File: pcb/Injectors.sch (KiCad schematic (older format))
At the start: 48 parts, among them Q1 VND14NV04, Q2 VND14NV04, Q3 VND14NV04, Q4 VND14NV04, Q5 VND14NV04, Q6 VND14NV04, Q7 VND14NV04, Q8 VND14NV04

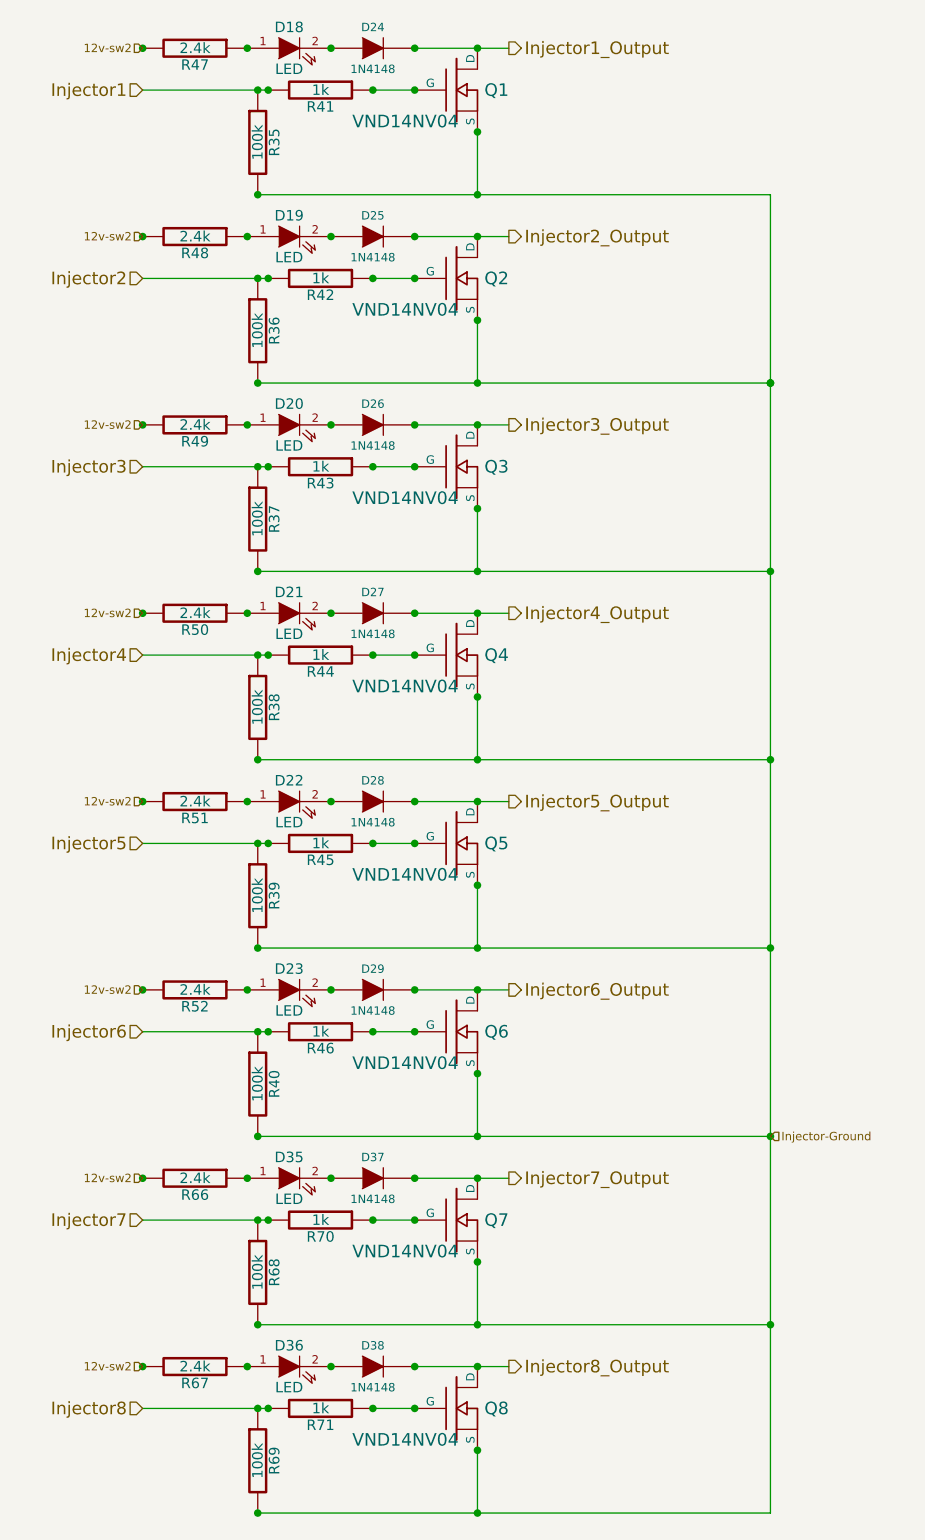
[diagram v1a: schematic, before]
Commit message: Updated schematics, PDFs and PNGs with lumpensack2003 suggestions
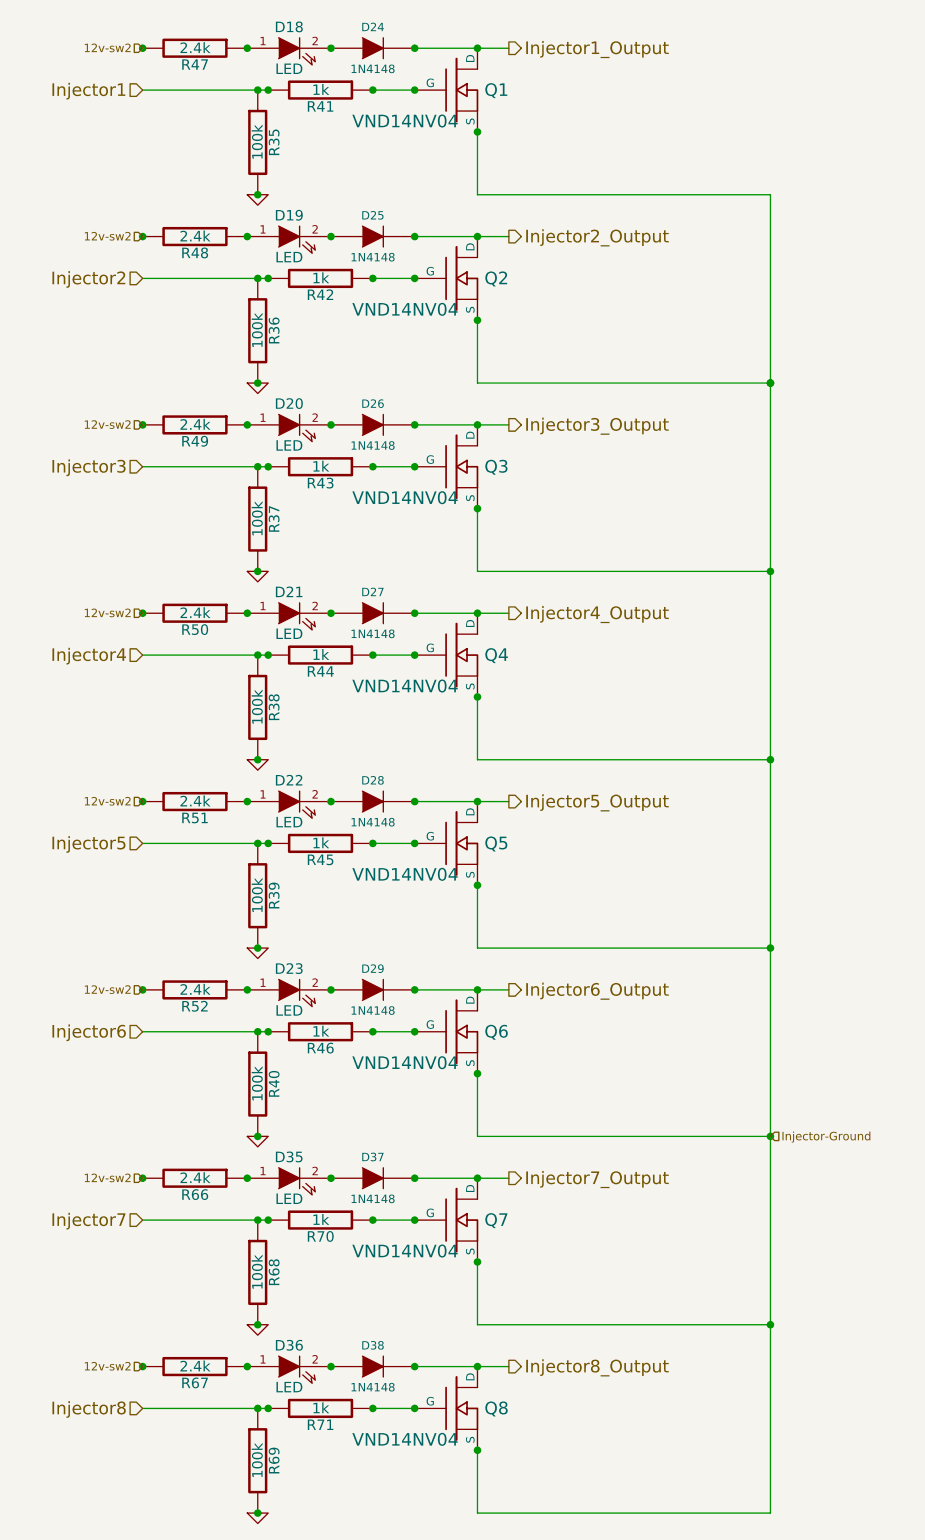
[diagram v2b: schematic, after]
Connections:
- net Injector-Ground: no longer R35.2, R36.2, R37.2, R38.2, R39.2, R40.2, R68.2, R69.2
- new net GND: R35.2, R36.2, R37.2, R38.2, R39.2, R40.2, R68.2, R69.2
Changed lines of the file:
@@
-EESchema Schematic File Version 2  date Sun 05 Feb 2012 11:20:52 AM EST
+EESchema Schematic File Version 2  date Sun 05 Feb 2012 10:59:48 PM EST
+LIBS:opto
+LIBS:Jaguar
 LIBS:power
-LIBS:device
-LIBS:transistors
-LIBS:conn
-LIBS:linear
-LIBS:regul
-LIBS:74xx
-LIBS:analog_switches
-LIBS:interface
-LIBS:opto
-LIBS:contrib
-LIBS:Jaguar
 LIBS:Jaguar-cache
 EELAYER 24  0
@@
 Sheet 6 7
 Title "Jaguar PCB for FreeEMS"
-Date "5 feb 2012"
+Date "6 feb 2012"
 Rev "A.2"
 Comp "diyefi.org"
@@
 Comment4 ""
 $EndDescr
+$Comp
+L GND #PWR063
+U 1 1 4F2F3F04
+P 2950 5000
+F 0 "#PWR063" H 2950 5000 30  0001 C CNN
+F 1 "GND" H 2950 4930 30  0001 C CNN
+	1    2950 5000
+	1    0    0    -1
+$EndComp
+$Comp
+L GND #PWR064
+U 1 1 4F2F3ECC
+P 2950 2300
+F 0 "#PWR064" H 2950 2300 30  0001 C CNN
+F 1 "GND" H 2950 2230 30  0001 C CNN
+	1    2950 2300
+	1    0    0    -1
+$EndComp
+$Comp
+L GND #PWR065
+U 1 1 4F2F3EC7
+P 2950 3200
+F 0 "#PWR065" H 2950 3200 30  0001 C CNN
+F 1 "GND" H 2950 3130 30  0001 C CNN
+	1    2950 3200
+	1    0    0    -1
+$EndComp
+$Comp
+L GND #PWR066
+U 1 1 4F2F3EC3
+P 2950 4100
+F 0 "#PWR066" H 2950 4100 30  0001 C CNN
+F 1 "GND" H 2950 4030 30  0001 C CNN
+	1    2950 4100
+	1    0    0    -1
+$EndComp
+$Comp
+L GND #PWR067
+U 1 1 4F2F3EBF
+P 2950 5900
+F 0 "#PWR067" H 2950 5900 30  0001 C CNN
+F 1 "GND" H 2950 5830 30  0001 C CNN
+	1    2950 5900
+	1    0    0    -1
+$EndComp
+$Comp
+L GND #PWR068
+U 1 1 4F2F3EBC
+P 2950 6800
+F 0 "#PWR068" H 2950 6800 30  0001 C CNN
+F 1 "GND" H 2950 6730 30  0001 C CNN
+	1    2950 6800
+	1    0    0    -1
+$EndComp
+$Comp
+L GND #PWR069
+U 1 1 4F2F3EB6
+P 2950 7700
+F 0 "#PWR069" H 2950 7700 30  0001 C CNN
+F 1 "GND" H 2950 7630 30  0001 C CNN
+	1    2950 7700
+	1    0    0    -1
+$EndComp
+Wire Wire Line
+	5400 7700 4000 7700
+Wire Wire Line
+	5400 5900 4000 5900
+Wire Wire Line
+	4000 4700 4000 5000
+Wire Wire Line
+	5400 4100 4000 4100
+Wire Wire Line
+	5400 2300 4000 2300
 Connection ~ 5400 2300
 Connection ~ 5400 6800
 Wire Wire Line
-	5400 1400 5400 7700
+	5400 7700 5400 1400
 Wire Wire Line
 	3700 1600 4150 1600
@@
 Connection ~ 2400 3400
 Connection ~ 2400 4300
-Connection ~ 4000 2300
 Connection ~ 5400 2300
-Wire Wire Line
-	5400 2300 2950 2300
-Connection ~ 4000 4100
 Connection ~ 5400 4100
-Wire Wire Line
-	5400 4100 2950 4100
-Wire Wire Line
-	5400 5900 2950 5900
 Wire Wire Line
 	2400 5400 3000 5400
@@
 Connection ~ 3300 700
 Wire Wire Line
-	4000 1400 4000 1100
+	4000 1100 4000 1400
 Connection ~ 2950 1400
 Wire Wire Line
@@
 Wire Wire Line
 	4000 4100 4000 3800
-Wire Wire Line
-	4000 4700 4000 5000
 Connection ~ 2950 5000
 Wire Wire Line
@@
 	4000 5900 4000 5600
 Connection ~ 4000 700
-Connection ~ 4000 5900
 Wire Wire Line
 	3000 4500 2400 4500
-Wire Wire Line
-	5400 5000 2950 5000
 Connection ~ 5400 5000
-Connection ~ 4000 5000
-Wire Wire Line
-	5400 3200 2950 3200
 Connection ~ 5400 3200
-Connection ~ 4000 3200
-Wire Wire Line
-	5400 1400 2950 1400
-Connection ~ 4000 1400
 Wire Wire Line
 	2400 3600 3000 3600
@@
 	3000 1800 2400 1800
 Connection ~ 3700 6100
-Connection ~ 4000 6800
-Wire Wire Line
-	4000 6800 4000 6500
+Wire Wire Line
+	4000 6500 4000 6800
 Connection ~ 2950 6800
 Wire Wire Line
@@
 	2400 6300 3000 6300
 Wire Wire Line
-	2950 6800 5400 6800
-Wire Wire Line
 	3700 6100 4150 6100
 Wire Wire Line
 	3700 7000 4150 7000
-Wire Wire Line
-	5400 7700 2950 7700
 Wire Wire Line
 	2400 7200 3000 7200
@@
 Wire Wire Line
 	4000 7700 4000 7400
-Connection ~ 4000 7700
 Connection ~ 3700 7000
+Wire Wire Line
+	4000 1400 5400 1400
+Wire Wire Line
+	4000 3200 5400 3200
+Wire Wire Line
+	4000 5000 5400 5000
+Wire Wire Line
+	4000 6800 5400 6800
+$Comp
+L GND #PWR070
+U 1 1 4F2F3E75
+P 2950 1400
+F 0 "#PWR070" H 2950 1400 30  0001 C CNN
+F 1 "GND" H 2950 1330 30  0001 C CNN
+	1    2950 1400
+	1    0    0    -1
+$EndComp
 Text HLabel 2400 7200 0    60   Input ~ 0
 Injector8

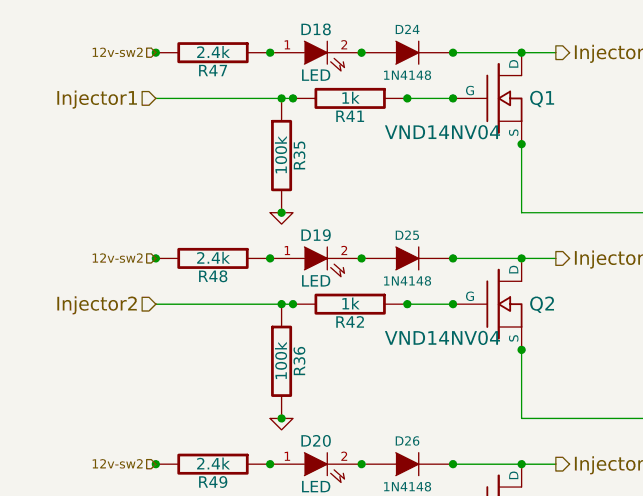
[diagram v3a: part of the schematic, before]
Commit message: Updated schematics for HCPL-061a Optocoupler
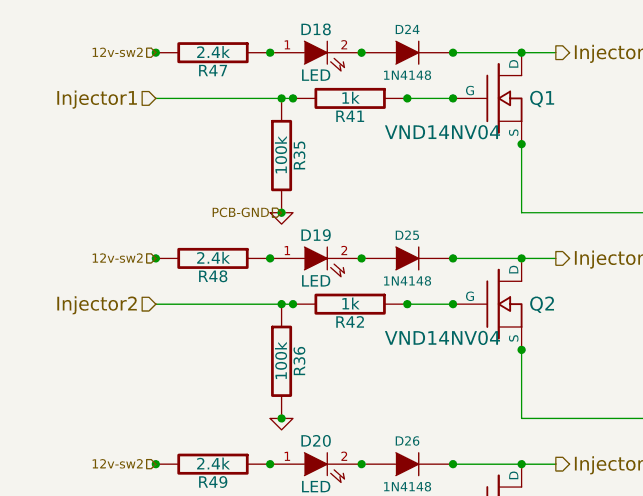
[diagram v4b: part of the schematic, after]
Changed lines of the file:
@@
-EESchema Schematic File Version 2  date Sat 18 Feb 2012 05:28:44 PM EST
+EESchema Schematic File Version 2  date Sun 19 Feb 2012 11:18:36 PM EST
 LIBS:opto
 LIBS:Jaguar
@@
 Sheet 6 7
 Title "Jaguar PCB for FreeEMS"
-Date "18 feb 2012"
+Date "20 feb 2012"
 Rev "A3"
 Comp "diyefi.org"
@@
 Comment4 ""
 $EndDescr
+Text HLabel 2950 1400 0    40   Input ~ 0
+PCB-GND
 $Comp
 L GND #PWR032
